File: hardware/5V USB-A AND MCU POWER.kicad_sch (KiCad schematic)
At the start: 45 parts, among them Q30 PMPB11EN,115, Q31 PMPB11EN,115, Q32 PMPB11EN,115, Q33 PMPB11EN,115, U2 LM5143, U5 NCP565ST12T3G

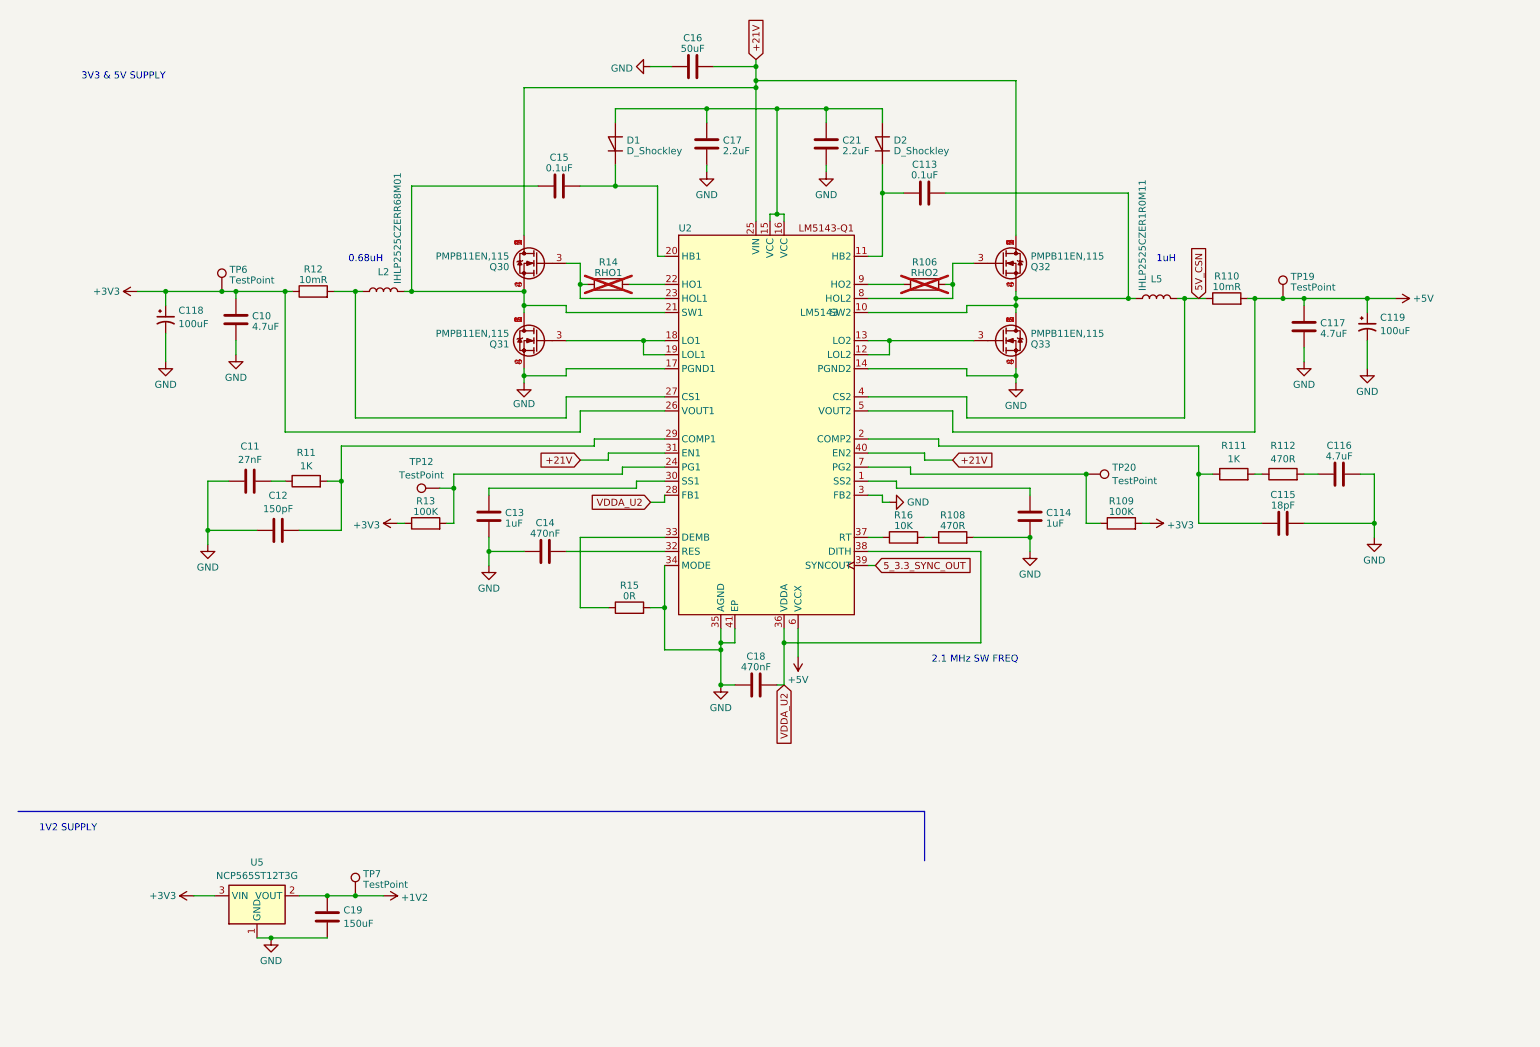
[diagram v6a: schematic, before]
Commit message: migrated to the esp32-s2 and starting new board revison
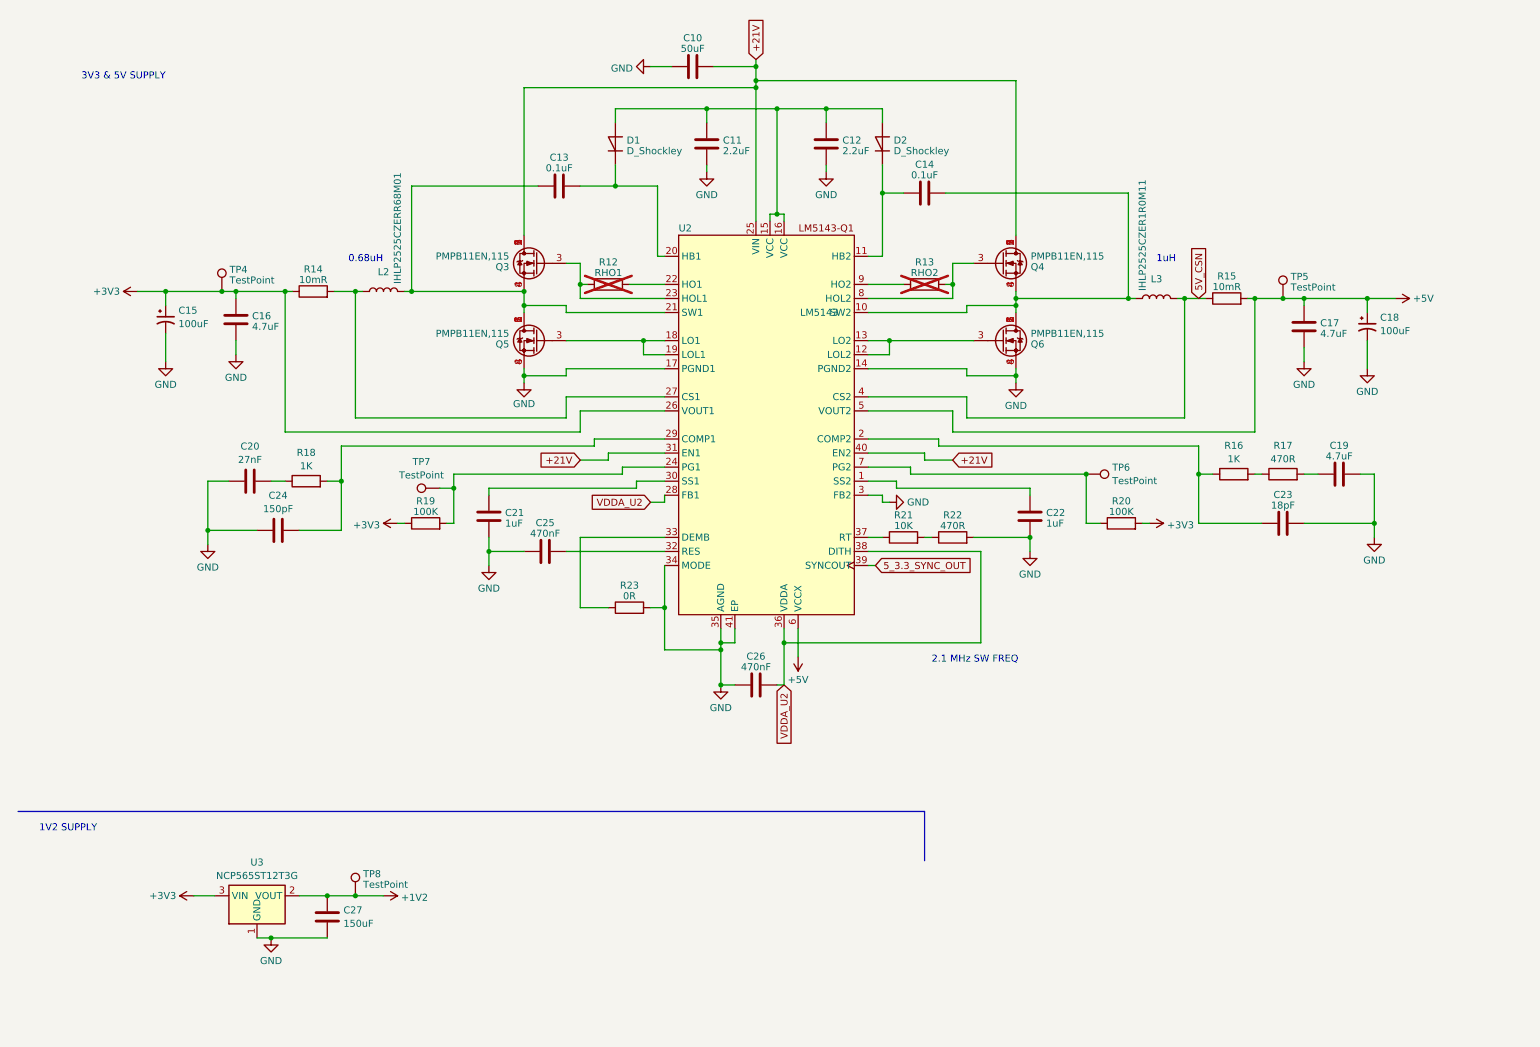
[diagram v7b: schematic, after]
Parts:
- C25: renamed from C14; footprint Capacitor_SMD:C_0805_2012Metric -> Capacitor_SMD:C_0603_1608Metric
- C26: renamed from C18; footprint Capacitor_SMD:C_0805_2012Metric -> Capacitor_SMD:C_0603_1608Metric
- TP5: renamed from TP19; footprint TestPoint:TestPoint_Pad_D1.5mm -> TestPoint:TestPoint_Pad_D1.0mm
- renumbered C16 to C10, C17 to C11, C21 to C12, C15 to C13, C113 to C14, C118 to C15, C10 to C16, C117 to C17, C119 to C18, C116 to C19, C11 to C20, C13 to C21, C114 to C22, C115 to C23, C12 to C24, C19 to C27, L5 to L3, Q30 to Q3, Q32 to Q4, Q31 to Q5, Q33 to Q6, R14 to R12, R106 to R13, R12 to R14, R110 to R15, R111 to R16, R112 to R17, R11 to R18, R13 to R19, R109 to R20, R16 to R21, R108 to R22, R15 to R23, TP6 to TP4, TP20 to TP6, TP12 to TP7, TP7 to TP8, U5 to U3
